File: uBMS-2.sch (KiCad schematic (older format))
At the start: 72 parts, among them J1 Micro_SD_Card_Det, Q1 2N7002, Q2 2N7002, Q3 NTD5865NL, U1 LM2576HVS-5, U2 ADS1115IDGS, U3 TLV1117-33, U4 TL431DBV, U5 ESP32-WROOM-32, U6 TSC2012IDT, U7 MCP23017_SS, U8 MCP23008-E_P, U9 VDMG10C0

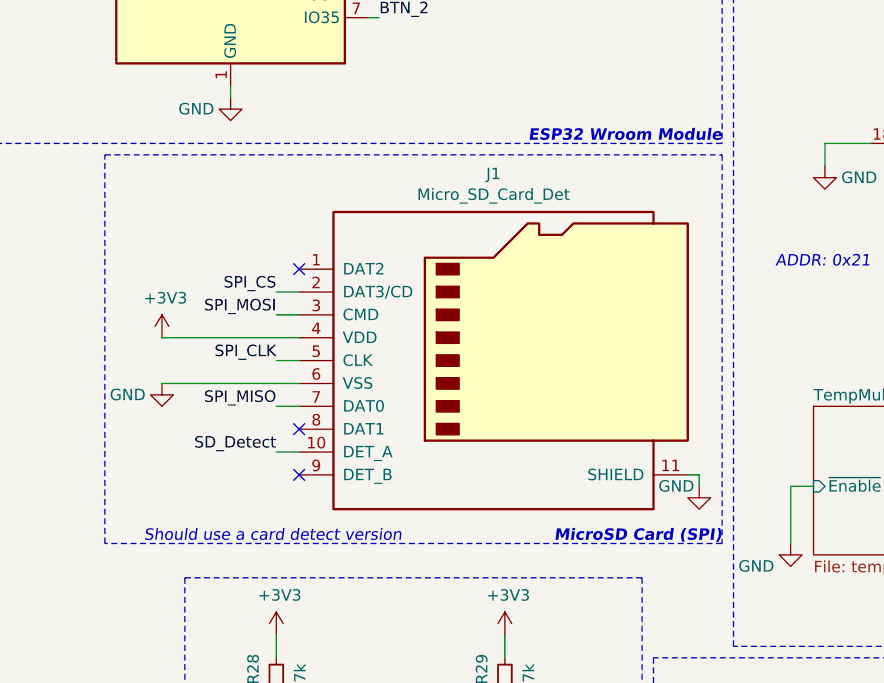
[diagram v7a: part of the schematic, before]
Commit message: Updated SD card adapter, again, for MEM2061
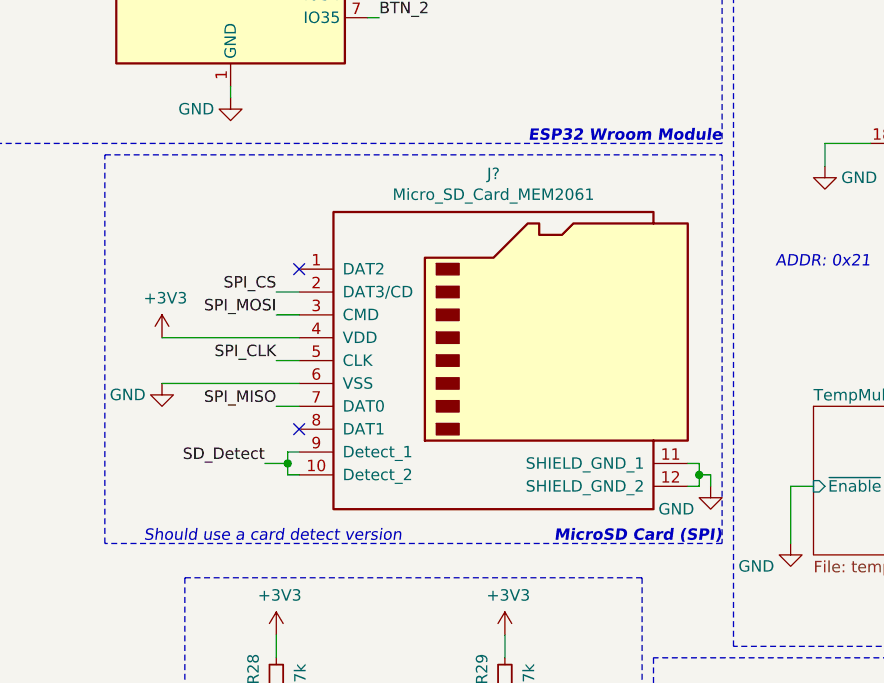
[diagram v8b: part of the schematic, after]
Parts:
- removed J1: Micro_SD_Card_Det, symbol Connector:Micro_SD_Card_Det
- added J?: Micro_SD_Card_MEM2061, symbol Connector:Micro_SD_Card_MEM2061
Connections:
- net +3V3: now also J?.4 (VDD)
- net GND: now also J?.11 (SHIELD_GND_1), J?.12 (SHIELD_GND_2), J?.6 (VSS)
- net SD_Detect: now also J?.10 (Detect_2), J?.9 (Detect_1)
- net SPI_CLK: now also J?.5 (CLK)
- net SPI_CS: now also J?.2 (DAT3/CD)
- net SPI_MISO: now also J?.7 (DAT0)
- net SPI_MOSI: now also J?.3 (CMD)
- no-connect marks 12 -> 11
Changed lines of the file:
@@
 L power:GND #PWR036
 U 1 1 5F23C6D3
-P 4600 5750
-F 0 "#PWR036" H 4600 5500 50  0001 C CNN
-F 1 "GND" H 4500 5750 50  0000 C CNN
-F 2 "" H 4600 5750 50  0001 C CNN
-F 3 "" H 4600 5750 50  0001 C CNN
-	1    4600 5750
-	1    0    0    -1
-$EndComp
-Wire Wire Line
-	4600 5750 4600 5700
-Wire Wire Line
-	4600 5700 4550 5700
+P 4650 5750
+F 0 "#PWR036" H 4650 5500 50  0001 C CNN
+F 1 "GND" H 4500 5650 50  0000 C CNN
+F 2 "" H 4650 5750 50  0001 C CNN
+F 3 "" H 4650 5750 50  0001 C CNN
+	1    4650 5750
+	1    0    0    -1
+$EndComp
+Wire Wire Line
+	4650 5750 4650 5700
+Wire Wire Line
+	4650 5700 4600 5700
 Text Label 3200 1900 0    50   ~ 0
 SPI_CS
@@
 Wire Wire Line
 	2250 5300 2850 5300
-NoConn ~ 2850 5500
 NoConn ~ 2850 4800
 Wire Notes Line
@@
 	6250 4700 6250 4650
 $Comp
-L Connector:Micro_SD_Card_Det J1
-U 1 1 5F28F4CE
-P 3750 5200
-F 0 "J1" H 3700 6017 50  0000 C CNN
-F 1 "Micro_SD_Card_Det" H 3700 5926 50  0000 C CNN
-F 2 "" H 5800 5900 50  0001 C CNN
-F 3 "https://www.hirose.com/product/en/download_file/key_name/DM3/category/Catalog/doc_file_id/49662/?file_category_id=4&item_id=195&is_series=1" H 3750 5300 50  0001 C CNN
-	1    3750 5200
-	1    0    0    -1
-$EndComp
-NoConn ~ 2850 5700
-$Comp
 L Device:R_Small R11
 U 1 1 5F2E72B5
@@
 Wire Wire Line
 	3800 3100 3150 3100
-Text Label 2750 5600 2    50   ~ 0
+Text Label 2700 5650 2    50   ~ 0
 SD_Detect
 Wire Wire Line
-	2750 5600 2850 5600
+	2700 5650 2800 5650
 NoConn ~ 1950 3100
 NoConn ~ 1950 3000
@@
 Wire Wire Line
 	6350 4950 6350 4650
+NoConn ~ 2850 5500
+$Comp
+L Connector:Micro_SD_Card_MEM2061 J?
+U 1 1 5F839F0E
+P 3700 5200
+F 0 "J?" H 3700 6017 50  0000 C CNN
+F 1 "Micro_SD_Card_MEM2061" H 3700 5926 50  0000 C CNN
+F 2 "" H 3800 6000 50  0001 C CNN
+F 3 "" H 3800 6000 50  0001 C CNN
+	1    3700 5200
+	1    0    0    -1
+$EndComp
+Wire Wire Line
+	2850 5600 2800 5600
+Wire Wire Line
+	2800 5600 2800 5650
+Wire Wire Line
+	2850 5700 2800 5700
+Wire Wire Line
+	2800 5700 2800 5650
+Connection ~ 2800 5650
+Wire Wire Line
+	4550 5650 4600 5650
+Wire Wire Line
+	4600 5650 4600 5700
+Wire Wire Line
+	4550 5750 4600 5750
+Wire Wire Line
+	4600 5750 4600 5700
+Connection ~ 4600 5700
 $EndSCHEMATC
